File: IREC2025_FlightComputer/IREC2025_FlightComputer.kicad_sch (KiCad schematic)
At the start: 36 parts, among them J1 Molex Microfit, U1 STM32U575VGTx, U2 TPS62153, U3 LP5912Q3.3DRVRQ1

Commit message: Schematics
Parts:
- added C27, C62: RVT1E101M0607, EasyEDA:CAP-SMD_BD6.3-L6.6-W6.6-LS7.2-R-RD, symbol EasyEDA:RVT1E101M0607
- added C52, C61: 2.2uF, PCM_JLCPCB:C_0402, symbol PCM_JLCPCB-Capacitors:0402,2.2uF
- added C53, C56: 100nF, PCM_JLCPCB:C_0402, symbol PCM_JLCPCB-Capacitors:0402,100nF
- added C54: 10pF, PCM_JLCPCB:C_0402, symbol PCM_JLCPCB-Capacitors:0402,10pF
- added C55: 1uF, PCM_JLCPCB:C_0402, symbol PCM_JLCPCB-Capacitors:0402,1uF
- added D4, D5: 3v3_led, LED_SMD:LED_0805_2012Metric, symbol Device:LED_Small_Filled
- added R21: 1kΩ, PCM_JLCPCB:R_0805, symbol PCM_JLCPCB-Resistors:0805,1kΩ
- added R22: 100kΩ, PCM_JLCPCB:R_0402, symbol PCM_JLCPCB-Resistors:0402,100kΩ
- added R25: 500Ω, PCM_JLCPCB:R_0805, symbol PCM_JLCPCB-Resistors:0805,1kΩ
- added U10, U11, U14, U15: NRVB120VLSFT1G, EasyEDA:SOD-123_L2.7-W1.6-LS3.7-RD-1, symbol EasyEDA:NRVB120VLSFT1G
- added U13: LP5912Q1.8DRVRQ1, EasyEDA:WSON-6_L2.0-W2.0-P0.65-BL-EP, symbol EasyEDA:LP5912Q1.8DRVRQ1
- added X1: 1XXD32000MBA, EasyEDA:OSC-SMD_4P-L2.0-W1.6-BL_1XXD, symbol EasyEDA:1XXD32000MBA
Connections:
- net +3.3V: now also U3.1 (OUT), C52.1, C53.1, R21.1, X1.4 (VCC); no longer C4.1, FB1.2, U1.22 (VDDA)
- net +5V: now also U10.2 (A), U14.2 (A)
- net GND: now also U1.20 (VREF-), U3.5 (GND), U3.7 (EP), C27.2, C52.2, C53.2, C54.2, C55.2, C56.2, C61.2, C62.2, D4.1 (K), D5.1 (K), R22.2, U13.5 (GND), U13.7 (PAD), X1.1 (GND), X1.2 (GND)
- net VBUS: now also U11.2 (A), U15.2 (A)
- net at U3.4 (EN): now also U3.6 (IN), C27.1, U10.1 (K), U11.1 (K)
- net VREF+: now reaches U1.21 (VREF+)
- net VREF+: now also C55.1
- new net: D4.2 (A), R21.2
- new net: D5.2 (A), R25.2
- new net: C62.1, U13.4 (EN), U13.6 (IN), U14.1 (K), U15.1 (K)
- new net +1V8: C61.1, R25.1, U13.1 (OUT)
- new net +3.3VA: C4.1, C56.1, FB1.2, U1.22 (VDDA)
- new net HSE_IN: C54.1, R22.1, X1.3 (Output)
- no-connect marks 2 -> 6
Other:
- added sheet GNSS (GNSS.kicad_sch)
- note added: "LDO 1.8V"
- note added: "LDO 3.3V"
- note added: "TCXO_HSE"
- moved on the sheet: C15, C16, C17, C18, D2, D3, J1, L1, R6, R7, R8, U2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

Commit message: update
21/3/2025
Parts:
- removed C54: 10pF, PCM_JLCPCB:C_0402, symbol PCM_JLCPCB-Capacitors:0402,10pF
- removed C61: 2.2uF, PCM_JLCPCB:C_0402, symbol PCM_JLCPCB-Capacitors:0402,2.2uF
- removed C62: RVT1E101M0607, EasyEDA:CAP-SMD_BD6.3-L6.6-W6.6-LS7.2-R-RD, symbol EasyEDA:RVT1E101M0607
- removed D5: 3v3_led, LED_SMD:LED_0805_2012Metric, symbol Device:LED_Small_Filled
- removed R22: 100kΩ, PCM_JLCPCB:R_0402, symbol PCM_JLCPCB-Resistors:0402,100kΩ
- removed R25: 500Ω, PCM_JLCPCB:R_0805, symbol PCM_JLCPCB-Resistors:0805,1kΩ
- removed U13: LP5912Q1.8DRVRQ1, EasyEDA:WSON-6_L2.0-W2.0-P0.65-BL-EP, symbol EasyEDA:LP5912Q1.8DRVRQ1
- removed U14, U15: NRVB120VLSFT1G, EasyEDA:SOD-123_L2.7-W1.6-LS3.7-RD-1, symbol EasyEDA:NRVB120VLSFT1G
- added C1: 100pF, PCM_JLCPCB:C_0402, symbol PCM_JLCPCB-Capacitors:0402,100pF
- added C12: 1uF, PCM_JLCPCB:C_0402, symbol PCM_JLCPCB-Capacitors:0402,1uF
- added C28: 100uF, PCM_JLCPCB:C_CASE-B-3528-21(mm), symbol PCM_JLCPCB-Capacitors:CASE-B-3528-21(mm),100uF
- added PWM1: Conn_01x03_Pin, Connector_Molex:Molex_Micro-Fit_3.0_43650-0315_1x03_P3.00mm_Vertical, symbol Connector:Conn_01x03_Pin
- added Pyro_A1, Pyro_B1, Pyro_C1: Molex Microfit, Connector_Molex:Molex_Micro-Fit_3.0_43650-0215_1x02_P3.00mm_Vertical, symbol Connector:Conn_01x02_Socket
- added Q1, Q2: SI7232DN-T1-GE3, EasyEDA:POWER-1212-8_L3.3-W3.3-P0.66-LS3.3-BL, symbol EasyEDA:SI7232DN-T1-GE3
- added R11, R16, R17: 3.3kΩ, PCM_JLCPCB:R_0402, symbol PCM_JLCPCB-Resistors:0402,3.3kΩ
- added R12, R13, R14, R15: 470Ω, PCM_JLCPCB:R_0402, symbol PCM_JLCPCB-Resistors:0402,470Ω
- added U9: SN74HCT125DR, EasyEDA:SOIC-14_L8.7-W3.9-P1.27-LS6.0-BL, symbol EasyEDA:SN74HCT125DR
- J1: footprint (none) -> Connector_Molex:Molex_Micro-Fit_3.0_43650-0215_1x02_P3.00mm_Vertical
- renumbered C53 to C13, C2 to C14, C3 to C15, C4 to C16, C15 to C17, C13 to C18, C14 to C19, C56 to C2, C16 to C20, C52 to C21, C27 to C23, C18 to C25, C1 to C26, C17 to C27, C55 to C3, C12 to C4, D3 to D1, D1 to D2, D2 to D3, R6 to R1, R8 to R10, R7 to R2, R1 to R3, R2 to R4, R3 to R6, R4 to R7, R21 to R8, U10 to U2, U11 to U4, U3 to U5, U2 to U8
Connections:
- net +3.3V: now also C12.1, C28.1, U9.14 (VCC)
- net +5V: now also PWM1.1 (Pin_1)
- net GND: now also C12.2, C28.2, PWM1.2 (Pin_2), Q1.1 (S1), Q1.3 (S2), Q2.1 (S1), R11.2, R12.2, R13.2, R14.2, R15.2, R16.2, R17.2, U9.7 (GND)
- net GNSS_INT: now also U1.26 (PA3); no longer U1.25 (PA2)
- net HSE_IN: now also C1.2; no longer X1.3 (Output)
- net VBAT+: now also Pyro_A1.2 (Pin_2), Pyro_B1.2 (Pin_2), Pyro_C1.2 (Pin_2)
- net GNSS_RX: now reaches U1.23 (PA0)
- net GNSS_TX: now reaches U1.24 (PA1)
- net LoRa_NSS: now reaches U1.29 (PA4)
- net LoRa_SCLK: now reaches U1.30 (PA5)
- net LoRa_MISO: now reaches U1.31 (PA6)
- net LoRa_MOSI: now reaches U1.32 (PA7)
- net ADXL_NSS: now reaches U1.51 (PB12)
- net ADXL_SCLK: now reaches U1.52 (PB13)
- net ADXL_MISO: now reaches U1.53 (PB14)
- net ADXL_MOSI: now reaches U1.54 (PB15)
- net MS5607_CS: now reaches U1.71 (PA12)
- net SPI3_SCLK: now reaches U1.78 (PC10)
- net SPI3_MISO: now reaches U1.79 (PC11)
- net SPI3_MOSI: now reaches U1.80 (PC12)
- net BMI_accel_INT1: now reaches U1.81 (PD0)
- net BMI_GYRO_INT1: now reaches U1.82 (PD1)
- new net: C1.1, X1.3 (Output)
- new net: Pyro_C1.1 (Pin_1), Q2.7 (D1), Q2.8 (D1)
- new net: Pyro_A1.1 (Pin_1), Q1.7 (D1), Q1.8 (D1)
- new net: Pyro_B1.1 (Pin_1), Q1.5 (D2), Q1.6 (D2)
- new net GNSS_RST: U1.25 (PA2)
- new net PWM_A: U9.2 (1A)
- new net PWM_B: U9.4 (~{2OE})
- new net PWM_C: U9.9 (3A)
- new net PWM_D: U9.12 (4A)
- new net PWM_PD: R12.1, R13.1, R14.1, R15.1, U9.1 (~{1OE}), U9.10 (~{3OE}), U9.13 (~{4OE}), U9.5 (2A)
- new net PYRO_A: Q1.2 (G1), R16.1, U9.3 (1Y)
- new net PYRO_B: Q1.4 (G2), R17.1, U9.6 (2Y)
- new net PYRO_C: Q2.2 (G1), R11.1, U9.8 (3Y)
- new net SERVO_A: PWM1.3 (Pin_3), U9.11 (4Y)
- no-connect marks 6 -> 8
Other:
- note added: "PWM level shifting (TenderDescender & Pyro)"
- note added: "Pyro connectors"
- note added: "Servo Connector"
- note removed: "LDO 1.8V"
- moved on the sheet: C10, C11, C13, C14, C15, C16, C17, C18, C19, C2, C20, C21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

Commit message: Updated 22/3/2025
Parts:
- added C22: 100nF, PCM_JLCPCB:C_0402, symbol PCM_JLCPCB-Capacitors:0402,100nF
- added J2: BOOT0, Connector_PinHeader_2.54mm:PinHeader_1x03_P2.54mm_Vertical, symbol Connector:Conn_01x03_Pin
- added J3: SWD, Connector_PinHeader_2.54mm:PinHeader_1x04_P2.54mm_Vertical, symbol Connector:Conn_01x04_Pin
- added R9: 10kΩ, PCM_JLCPCB:R_0402, symbol PCM_JLCPCB-Resistors:0402,10kΩ
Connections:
- net MS5607_CS is gone; now on net USB_DP: U1.71 (PA12)
- net +3.3V: now also J3.1 (Pin_1)
- net ADXL_MISO: no longer U1.53 (PB14)
- net ADXL_MOSI: no longer U1.54 (PB15)
- net ADXL_NSS: no longer U1.51 (PB12)
- net ADXL_SCLK: no longer U1.52 (PB13)
- net BMI_GYRO_INT1: now also U1.84 (PD3); no longer U1.82 (PD1)
- net BMI_accel_INT1: now also U1.83 (PD2); no longer U1.81 (PD0)
- net GND: now also C22.2, J2.3 (Pin_3), J3.4 (Pin_4)
- net HSE_IN: now also U1.12 (PH0)
- net NRST: now also C22.1
- net USB_DN: now also U1.70 (PA11)
- net eMMC_CLK: now reaches U1.16 (PC1)
- net DAT7: now reaches U1.63 (PC6)
- net DAT6: now reaches U1.64 (PC7)
- net SWDIO: now reaches U1.72 (PA13)
- net SWDIO: now also J3.2 (Pin_2)
- net SWCLK: now reaches U1.76 (PA14)
- net SWCLK: now also J3.3 (Pin_3)
- net MS5607_NSS: now reaches U1.77 (PA15)
- net eMMC_CMD: now reaches U1.88 (PD7)
- net DAT2: now reaches U1.89 (PB3)
- net DAT3: now reaches U1.90 (PB4)
- net BOOT0: now reaches U1.94 (PH3)
- net BOOT0: now also R9.2
- net DAT4: now reaches U1.95 (PB8)
- net DAT5: now reaches U1.96 (PB9)
- new net: J2.2 (Pin_2), R9.1
- new net +3V3: J2.1 (Pin_1)
- new net BMI_GYRO_CS: U1.81 (PD0)
- new net BMI_accel_CS: U1.82 (PD1)
- new net DAT0: U1.54 (PB15)
- new net DAT1: U1.53 (PB14)
- no-connect marks 8 -> 9
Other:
- note added: "Serial Wire Debug"
- note added: "place jumper cap"
- moved on the sheet: C1, C10, C11, C12, C13, C14, C15, C16, C17, C18, C19, C2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

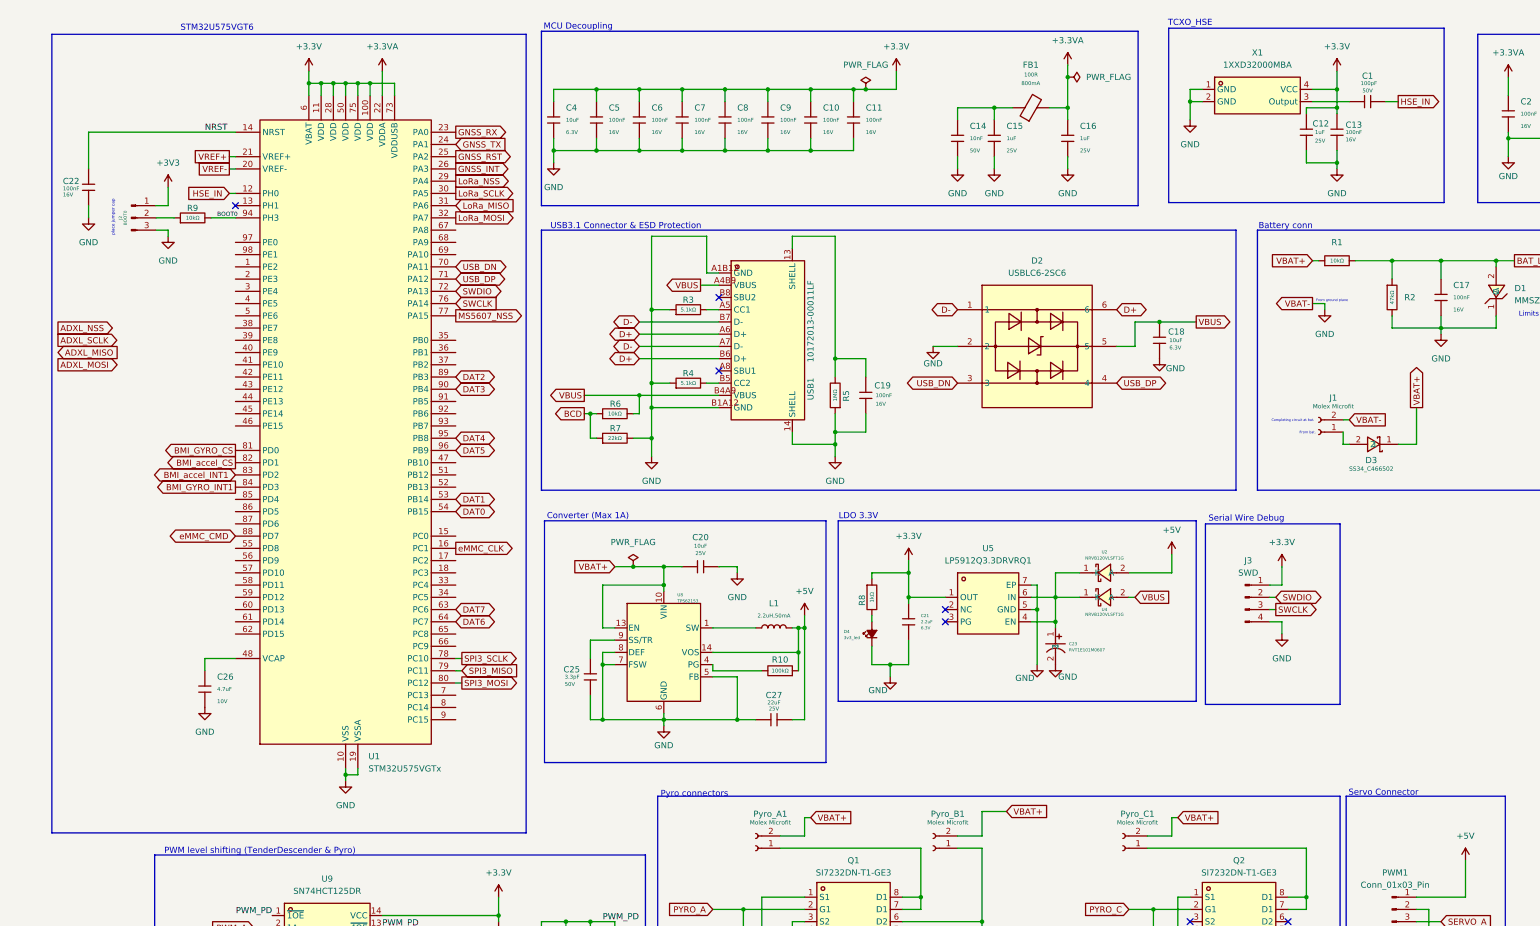
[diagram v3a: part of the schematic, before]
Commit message: Updated schematic + initiate layout
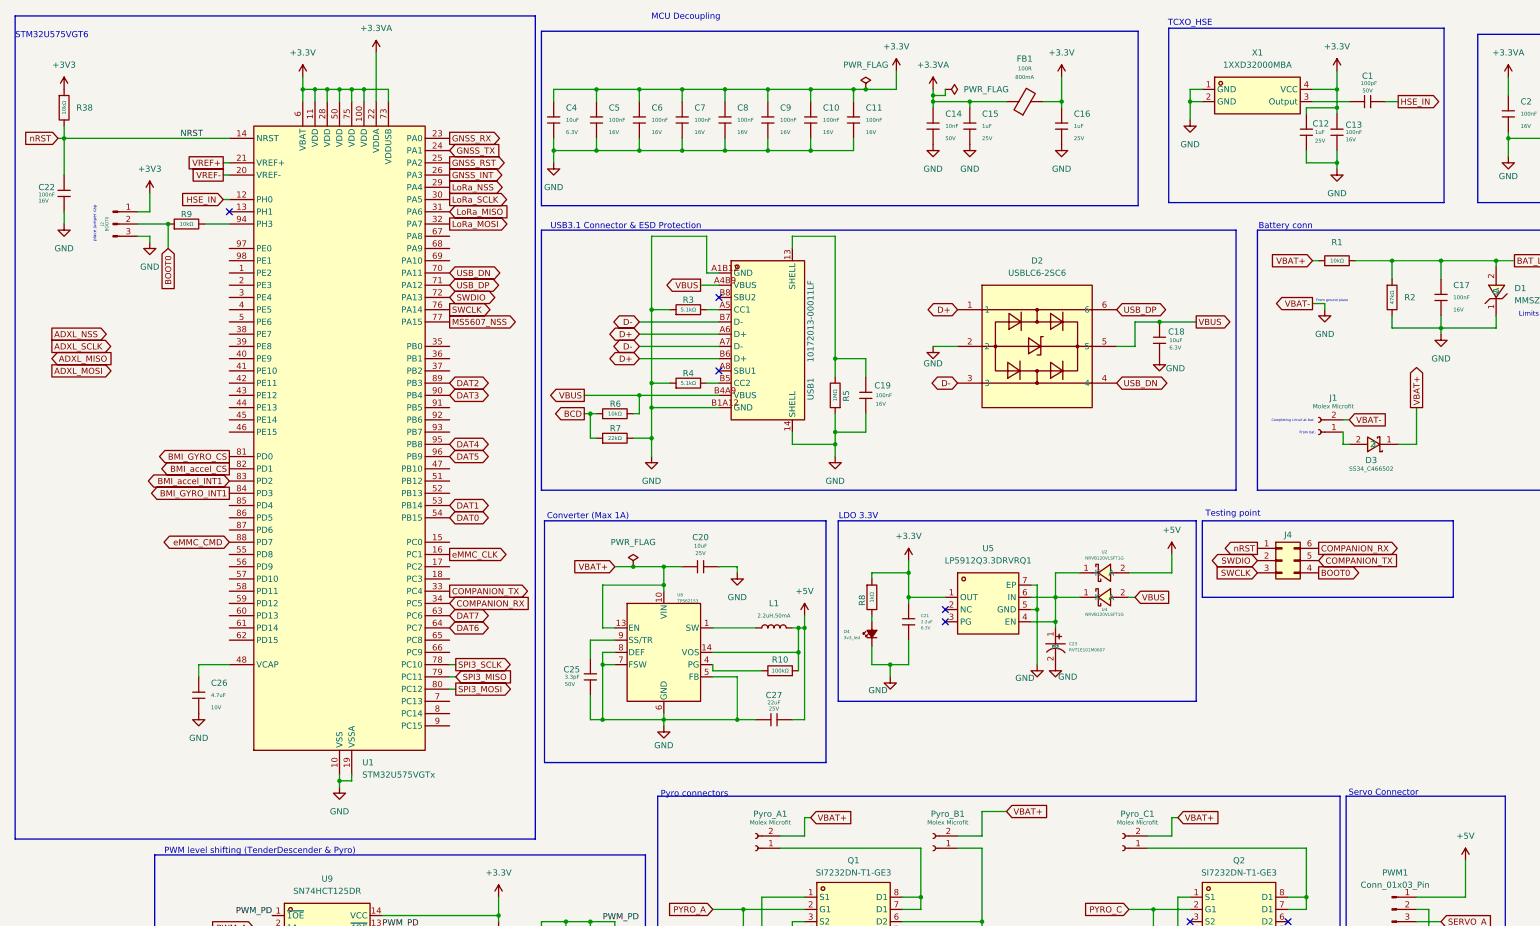
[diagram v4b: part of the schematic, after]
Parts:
- removed J3: SWD, Connector_PinHeader_2.54mm:PinHeader_1x04_P2.54mm_Vertical, symbol Connector:Conn_01x04_Pin
- added J4: Conn_02x03_Counter_Clockwise, Connector_PinHeader_2.54mm:PinHeader_2x03_P2.54mm_Vertical, symbol Connector_Generic:Conn_02x03_Counter_Clockwise
- added R38: 10kΩ, PCM_JLCPCB:R_0402, symbol PCM_JLCPCB-Resistors:0402,10kΩ
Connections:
- net +3.3V: now also C16.1, FB1.2
- net +3.3VA: now also C14.1, C15.1, FB1.1; no longer C16.1, FB1.2
- net +3V3: now also R38.1
- net BOOT0: now also J2.2 (Pin_2), R9.1, J4.4 (Pin_4); no longer R9.2, U1.94 (PH3)
- net D+: now also D2.1; no longer D2.6
- net D-: now also D2.3; no longer D2.1
- net SWCLK: now also J4.3 (Pin_3)
- net SWDIO: now also J4.2 (Pin_2)
- net USB_DN: now also D2.4; no longer D2.3
- net USB_DP: now also D2.6; no longer D2.4
- net COMPANION_TX: now reaches U1.33 (PC4)
- net COMPANION_TX: now also J4.5 (Pin_5)
- net COMPANION_RX: now reaches U1.34 (PC5)
- net COMPANION_RX: now also J4.6 (Pin_6)
- net NRST renamed nRST
- net nRST: now also J4.1 (Pin_1), R38.2
- new net: R9.2, U1.94 (PH3)
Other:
- note added: "Testing point"
- note removed: "Serial Wire Debug"
- moved on the sheet: C14, C15, C16, C22, C26, FB1, J2, R9, U1

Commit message: update idk
25/3/2025
starting to take shape (i guess)
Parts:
- removed L1: 2.2uH,50mA, PCM_JLCPCB:L_0805, symbol PCM_JLCPCB-Inductors:2.2uH,50mA
- added L1: 2.2uH,50mA, EasyEDA:IND-SMD_L4.0-W4.0_XFL4020-102MEB, symbol EasyEDA:XFL4020-472MEC
- D3: footprint EasyEDA:SMA_L4.4-W2.6-LS5.0-RD -> GNSS:DIOM7959X262N
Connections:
- net +5V: now also L1.2
- net BMI_accel_CS: now also U1.86 (PD5); no longer U1.82 (PD1)
- net BMI_accel_INT1: now also U1.87 (PD6); no longer U1.83 (PD2)
- net COMPANION_RX: now also U1.33 (PC4); no longer U1.34 (PC5)
- net COMPANION_TX: now also U1.34 (PC5); no longer U1.33 (PC4)
- net at U8.1 (SW), U8.2 (SW), U8.3 (SW): now also L1.1
- net MMC_SCL: now reaches U1.59 (PD12)
- net MMC_SDA: now reaches U1.60 (PD13)
- net BMI_GYRO_INT2: now reaches U1.85 (PD4)
- net TMP_SCL: now reaches U1.92 (PB6)
- net TMP_SDA: now reaches U1.93 (PB7)

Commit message: checkpoint
before the great layout change
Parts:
- removed C19, C22: 100nF, PCM_JLCPCB:C_0402, symbol PCM_JLCPCB-Capacitors:0402,100nF
- removed C23: RVT1E101M0607, EasyEDA:CAP-SMD_BD6.3-L6.6-W6.6-LS7.2-R-RD, symbol EasyEDA:RVT1E101M0607
- removed C25: 3.3pF, PCM_JLCPCB:C_0402, symbol PCM_JLCPCB-Capacitors:0402,3.3pF
- removed C27: 22uF, PCM_JLCPCB:C_0805, symbol PCM_JLCPCB-Capacitors:0805,22uF
- removed C28: 100uF, PCM_JLCPCB:C_CASE-B-3528-21(mm), symbol PCM_JLCPCB-Capacitors:CASE-B-3528-21(mm),100uF
- removed D4: 3v3_led, LED_SMD:LED_0805_2012Metric, symbol Device:LED_Small_Filled
- removed Pyro_C1: Molex Microfit, Connector_Molex:Molex_Micro-Fit_3.0_43650-0215_1x02_P3.00mm_Vertical, symbol Connector:Conn_01x02_Socket
- removed Q2: SI7232DN-T1-GE3, EasyEDA:POWER-1212-8_L3.3-W3.3-P0.66-LS3.3-BL, symbol EasyEDA:SI7232DN-T1-GE3
- removed R11: 3.3kΩ, PCM_JLCPCB:R_0402, symbol PCM_JLCPCB-Resistors:0402,3.3kΩ
- removed R5: 1MΩ, PCM_JLCPCB:R_0402, symbol PCM_JLCPCB-Resistors:0402,1MΩ
- removed R6: 10kΩ, PCM_JLCPCB:R_0402, symbol PCM_JLCPCB-Resistors:0402,10kΩ
- removed R7: 22kΩ, PCM_JLCPCB:R_0402, symbol PCM_JLCPCB-Resistors:0402,22kΩ
- removed R8: 1kΩ, PCM_JLCPCB:R_0805, symbol PCM_JLCPCB-Resistors:0805,1kΩ
- added C22: 100nF, PCM_JLCPCB:C_0402, symbol Device:C_Small
- added C23: 22uF, PCM_JLCPCB:C_0603, symbol PCM_JLCPCB-Capacitors:0603,22uF
- added C24: 10uF, PCM_JLCPCB:C_0805, symbol PCM_JLCPCB-Capacitors:1206,10uF
- added C25: GJM1555C1H3R3BB01D, EasyEDA:C0402, symbol EasyEDA:GJM1555C1H3R3BB01D
- added C28, C74: 100uF, EasyEDA:CAP-SMD_L3.2-W1.6, symbol EasyEDA:T520A107M006ATE070
- added C70: 100nF, PCM_JLCPCB:C_0402, symbol PCM_JLCPCB-Capacitors:1206,100nF
- added H1, H2, H3, H4: MountingHole_Pad, MountingHole:MountingHole_3.2mm_M3_DIN965_Pad, symbol Mechanical:MountingHole_Pad
- added SERVO2: Conn_01x03_Pin, Connector_Molex:Molex_Micro-Fit_3.0_43650-0315_1x03_P3.00mm_Vertical, symbol Connector:Conn_01x03_Pin
- C1: name (none) -> CC0402JRNPO9BN101
- C10, C13, C17, C2: name (none) -> GRM155R71H104KE14D
- C12, C3: name (none) -> GRM155R70J105KA12D
- C14: name (none) -> C0402C103K4RECTU
- C18: name (none) -> GRM155R61A106ME11D
- C20: footprint PCM_JLCPCB:C_0603 -> PCM_JLCPCB:C_0805; Temperature Coefficient X5R -> X7R; namw (none) -> CL21B106KOQNNNE
- C21: footprint PCM_JLCPCB:C_0402 -> PCM_JLCPCB:C_0603; Name (none) -> CL10B225KP8NNNC; Temperature Coefficient X5R -> X7R
- C26: footprint PCM_JLCPCB:C_0402 -> PCM_JLCPCB:C_0603; Temperature Coefficient X5R -> X7R; name (none) -> GRM188Z71A475ME15D
- C4: footprint PCM_JLCPCB:C_0402 -> PCM_JLCPCB:C_0805
- L1: namw (none) -> 74437349047
- R1: name (none) -> RC0402JR-0710KL
- R10: name (none) -> RC0402JR-07100KL
- R12: Name (none) -> RC0402FR-07470RL x 4
- R16, R17: name (none) -> ERA-2AEB332X
- R2: name (none) -> RC0402FR-0747KL
- R3, R4: Name (none) -> ERA-2AEB512X
- R38, R9: Name (none) -> RC0402JR-0710KL
- renumbered Pyro_A1 to Pyro_CH1, Pyro_B1 to Pyro_CH2, PWM1 to SERVO1
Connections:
- net +3V3 is gone; now on net +3.3V: J2.1 (Pin_1), R38.1
- net PYRO_C is gone; now on net SERVO_A: U9.8 (3Y)
- net VREF+ is gone; now on net +3.3VA: C3.1, U1.21 (VREF+)
- net +3.3V: no longer U9.14 (VCC)
- net +5V: now also U9.14 (VCC), C23.2, C28.1, SERVO2.1 (Pin_1)
- net ADXL_MISO: now also U1.17 (PC2)
- net ADXL_MOSI: now also U1.18 (PC3)
- net ADXL_NSS: now also U1.51 (PB12)
- net ADXL_SCLK: now also U1.47 (PB10)
- net BAT_LEVEL: now also U1.97 (PE0)
- net BMI_GYRO_INT1: now also U1.83 (PD2); no longer U1.84 (PD3)
- net BMI_GYRO_INT2: now also U1.84 (PD3); no longer U1.85 (PD4)
- net BMI_accel_CS: now also U1.85 (PD4); no longer U1.86 (PD5)
- net BMI_accel_INT1: now also U1.86 (PD5); no longer U1.87 (PD6)
- net DAT0: now also U1.53 (PB14); no longer U1.54 (PB15)
- net DAT1: now also U1.54 (PB15); no longer U1.53 (PB14)
- net DAT6: now also U1.63 (PC6); no longer U1.64 (PC7)
- net DAT7: now also U1.64 (PC7); no longer U1.63 (PC6)
- net GND: now also USB1.13 (SHELL), C22.2, C23.1, C24.2, C25.1, C28.2, C70.2, C74.2, H1.1, H2.1, H3.1, H4.1, SERVO2.2 (Pin_2)
- net PWM_A: now also U1.2 (PE3)
- net PWM_B: now also U1.3 (PE4)
- net PWM_C: now also U1.4 (PE5)
- net PWM_D: now also U1.5 (PE6)
- net SERVO_A: no longer U9.11 (4Y)
- net VBAT+: now also C24.1, C70.1
- net nRST: now also C22.1
- net at U8.9 (SS/TR): now also C25.2
- net at U2.1 (K), U4.1 (K), U5.4 (EN)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: now also C74.1
- net BUZZER: now reaches U1.40 (PE9)
- net ADXL_INT2: now reaches U1.41 (PE10)
- net ADXL_INT1: now reaches U1.42 (PE11)
- net LoRa_RST: now reaches U1.43 (PE12)
- net GNSS_SAFEBOOT: now reaches U1.44 (PE13)
- net BUSY: now reaches U1.52 (PB13)
- net LORA_DIO3: now reaches U1.55 (PD8)
- net RST_n: now reaches U1.58 (PD11)
- net ANT_SW: now reaches U1.69 (PA10)
- net TMP_ALERT: now reaches U1.91 (PB5)
- new net BMI_accel_INT2: U1.87 (PD6)
- new net SERVO_B: SERVO2.3 (Pin_3), U9.11 (4Y)
- no-connect marks 9 -> 27
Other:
- note added: "CL21B106KOQNNNE"
- note added: "Companion"
- note added: "GRM155R70J105KA12D"
- note added: "GRM155R71H104KE14D"
- note added: "Pyro connectors (COTS EAGLE and COTS TENDER)"
- note added: "Pyro_CH1 (COTS TENDER)"
- note added: "Pyro_CH2 (EAGLE)"
- note added: "SERVO_CH1 (DODO-separation)"
- note added: "SERVO_CH1 (DODO_SEPARATION)"
- note added: "SERVO_CH2 (LEASH)"
- note added: "Servo Connectors (SRAD DODO and SRAD LEASH)"
- note removed: "Pyro connectors"
- note removed: "Servo Connector"
- note removed: "Testing point"
- moved on the sheet: SERVO1
